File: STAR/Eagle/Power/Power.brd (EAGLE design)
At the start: 51 x 40.4 mm, 46 parts, among them J1 J30J-25, U1 LMR16020, U2 LMR16020, U3 LMR16020

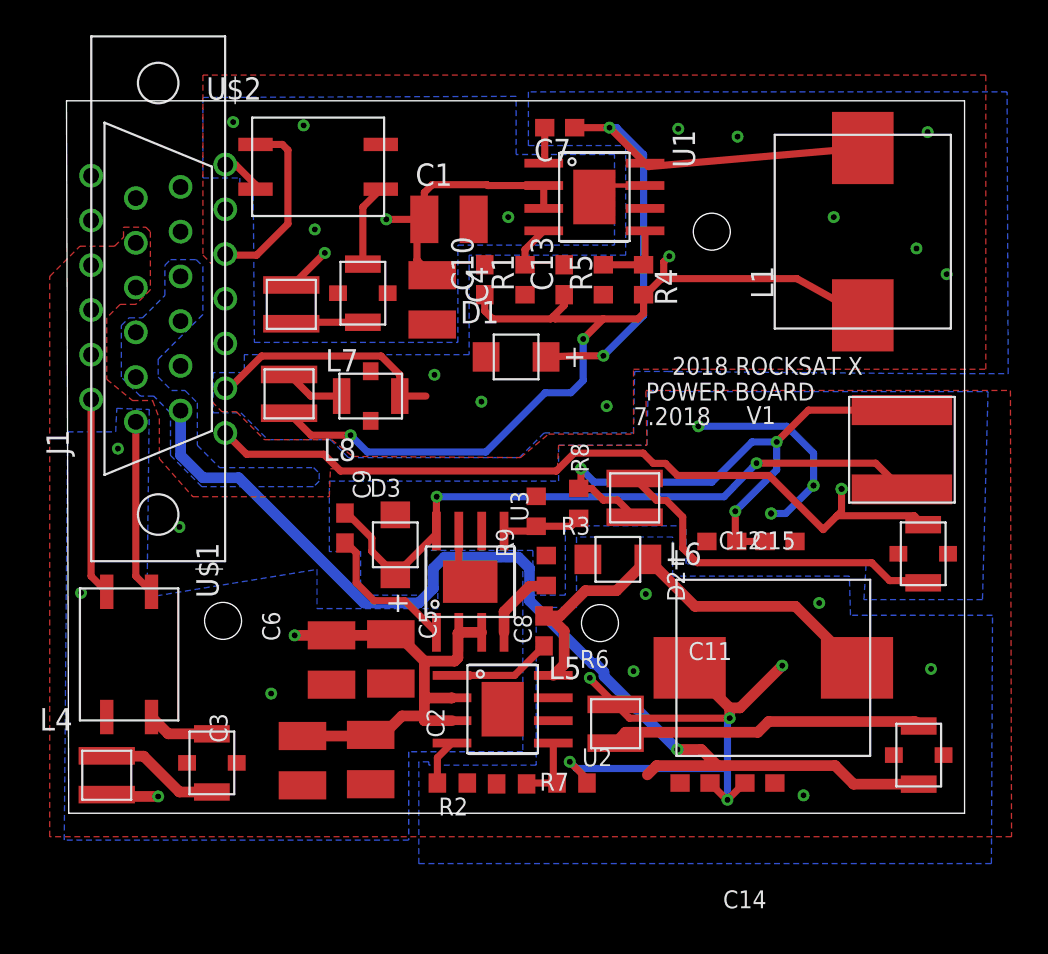
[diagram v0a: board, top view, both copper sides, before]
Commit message: reoriented capacitors on power board
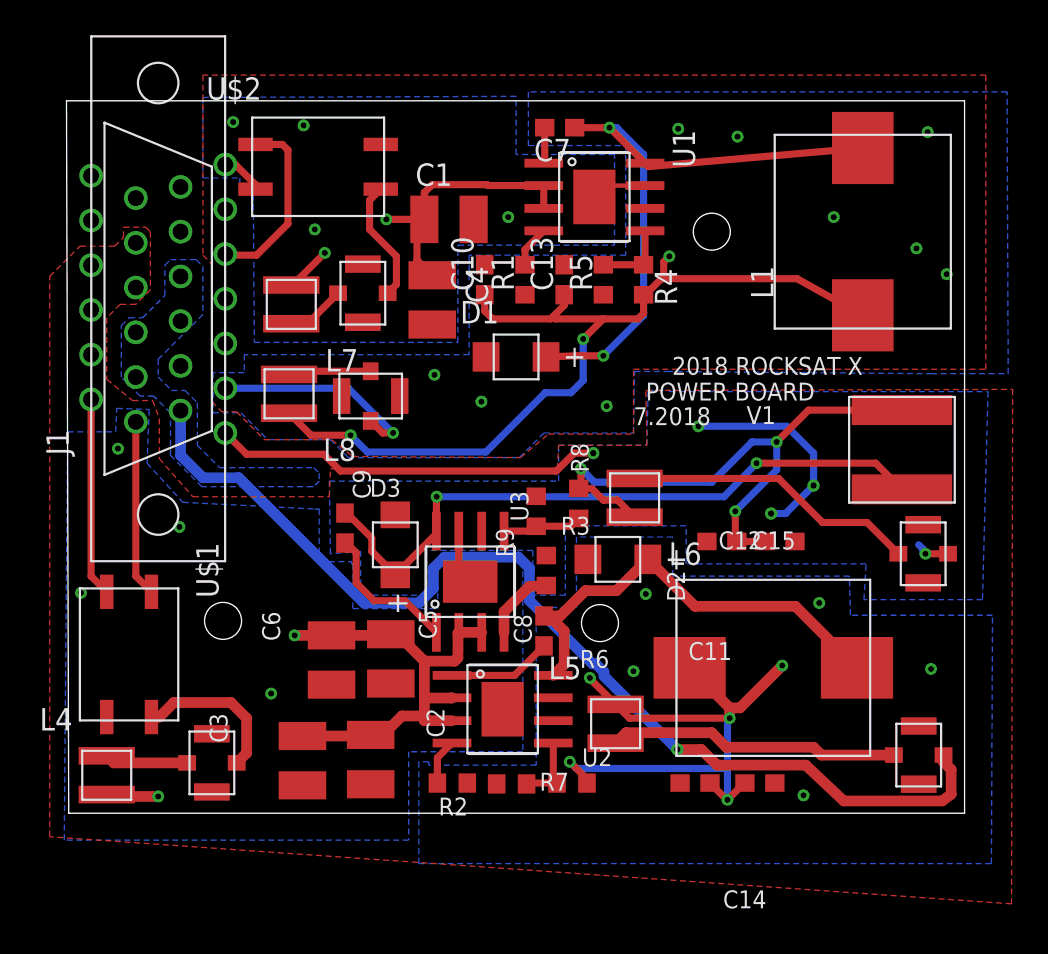
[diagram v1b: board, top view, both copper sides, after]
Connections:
- net 12V_FILT: now also U$7.P$4; no longer U$7.P$3
- net 3V3_FILT: now also U$5.P$4; no longer U$5.P$3
- net 5V_FILT: now also U$4.P$4; no longer U$4.P$2
- net GND: now also U$6.P$2, U$6.P$3; no longer U$6.P$4, U$6.P$5, U$7.P$4, U$7.P$5
- net GSE_GND: now also U$3.P$2, U$3.P$3, U$4.P$2, U$4.P$3, U$5.P$2, U$5.P$3; no longer U$3.P$4, U$3.P$5, U$4.P$4, U$4.P$5, U$5.P$4, U$5.P$5
- net N$28: now also U$1.P$4, U$3.P$4; no longer L4.P$1, U$3.P$2
- net N$29: now also U$6.P$5; no longer U$6.P$2
- net N$31: now also L4.P$1, U$3.P$5; no longer U$1.P$4, U$3.P$3
- net N$32: now also U$4.P$5; no longer U$4.P$3
- net N$33: now also U$5.P$5; no longer U$5.P$2
- net N$34: now also U$6.P$4; no longer U$6.P$3
- net N$35: now also U$7.P$5; no longer U$7.P$2
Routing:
- net 3V3_FILT: track 44.9 -> 24.2 mm, vias 1 -> 2
- net N$33: track 19.9 -> 16.7 mm
- net N$29: track 4.68 -> 7.00 mm
- net N$28: track 6.82 -> 8.88 mm
- net 12V_FILT: track 13.8 -> 12.1 mm, vias 0 -> 7
- net N$32: track 17.8 -> 16.6 mm
- net N$35: track 3.49 -> 4.71 mm
- net N$31: track 3.82 -> 4.73 mm
- net N$34: track 4.10 -> 3.37 mm
- net 5V_FILT: track 60.4 -> 61.0 mm
- added copper zone on layer 16, net 12V_FILT
- removed copper zone on layer 16, net +12V_FILT

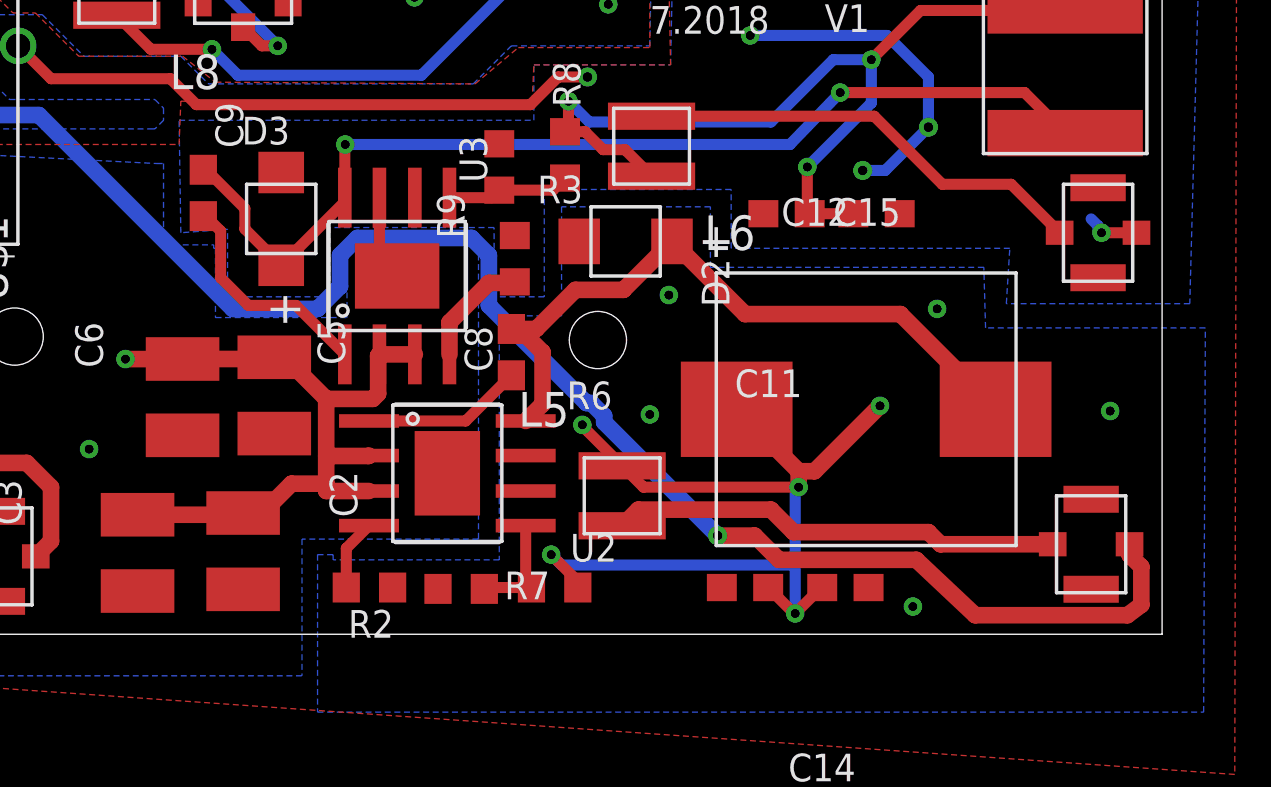
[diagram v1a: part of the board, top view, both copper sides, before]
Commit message: Fixed an air wire on the ground lines and a non-connection in the sketch
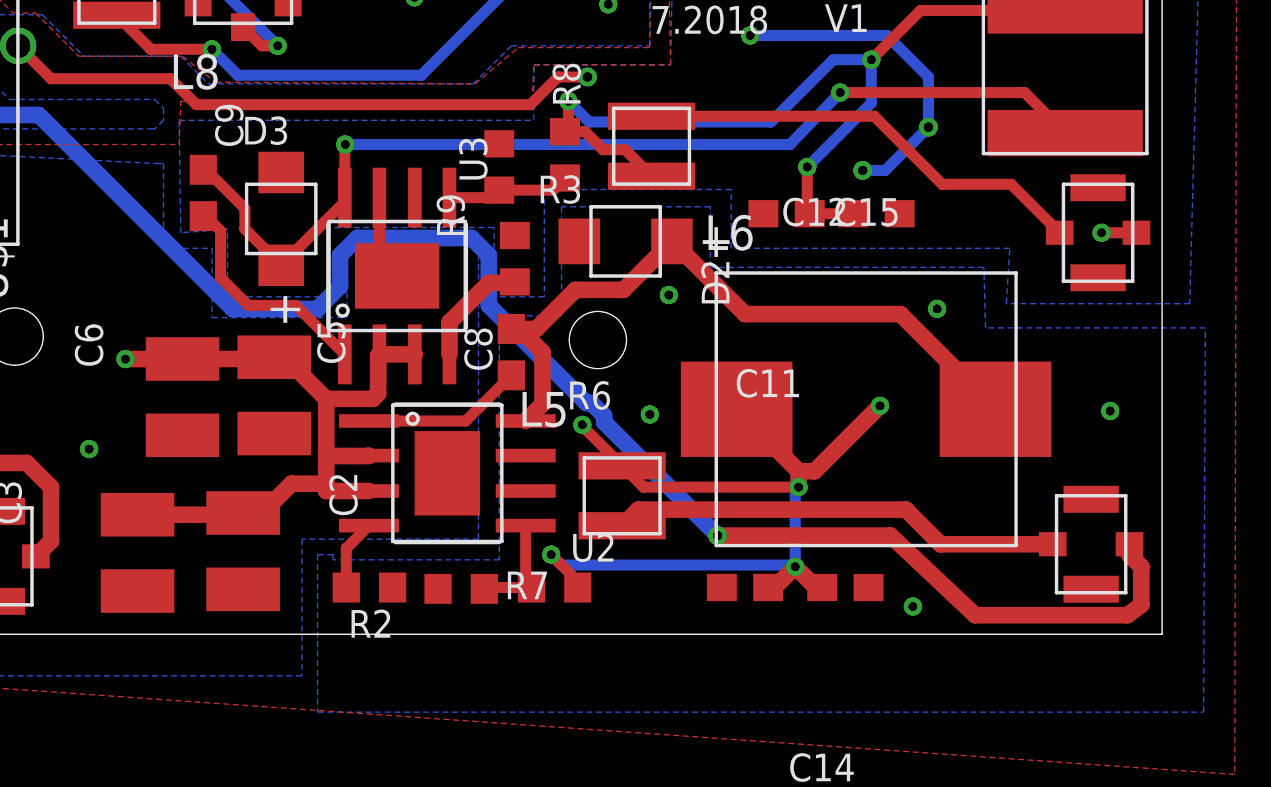
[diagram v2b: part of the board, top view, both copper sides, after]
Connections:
- removed net N$38: U$1.P$3
- net GND: now also U$7.P$3
- net GSE_GND: now also U$1.P$3
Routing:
- net +5V: track 34.9 -> 33.0 mm
- net 3V3_FILT: track 24.2 -> 23.5 mm
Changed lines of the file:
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@@
 <?xml version="1.0" encoding="utf-8"?>
 <!DOCTYPE eagle SYSTEM "eagle.dtd">
-<eagle version="7.6.0">
+<eagle version="9.1.0">
 <drawing>
 <settings>
 <setting alwaysvectorfont="no"/>
+<setting keepoldvectorfont="yes"/>
 <setting verticaltext="up"/>
 </settings>
@@
 <param name="dpMaxLengthDifference" value="10mm"/>
 <param name="dpGapFactor" value="2.5"/>
-<param name="checkGrid" value="0"/>
 <param name="checkAngle" value="0"/>
 <param name="checkFont" value="1"/>
 <param name="checkRestrict" value="1"/>
+<param name="checkStop" value="0"/>
+<param name="checkValues" value="0"/>
+<param name="checkNames" value="1"/>
+<param name="checkWireStubs" value="1"/>
+<param name="checkPolygonWidth" value="0"/>
 <param name="useDiameter" value="13"/>
 <param name="maxErrors" value="50"/>
@@
 <contactref element="U$6" pad="P$2"/>
 <contactref element="U$6" pad="P$3"/>
+<contactref element="U$7" pad="P$3"/>
 </signal>
 <signal name="N$1">
@@
 <via x="23.241" y="1.3335" extent="1-16" drill="0.3302"/>
 <via x="22.098" y="-3.429" extent="1-16" drill="0.3302"/>
-<via x="31.0515" y="-5.588" extent="1-16" drill="0.3302"/>
+<via x="31.0515" y="-3.8735" extent="1-16" drill="0.3302"/>
 <via x="34.163" y="2.032" extent="1-16" drill="0.3302"/>
 <wire x1="23.075" y1="-4.6355" x2="23.075" y2="-4.406" width="0.4064" layer="1"/>
@@
 <wire x1="23.241" y1="1.3335" x2="23.3885" y2="1.143" width="0.4064" layer="1"/>
 <wire x1="23.3885" y1="1.143" x2="24.7015" y2="-0.17" width="0.4064" layer="1"/>
-<wire x1="30.06" y1="-4.6355" x2="31.0125" y2="-5.588" width="0.4064" layer="1"/>
-<wire x1="31.0125" y1="-5.588" x2="31.0515" y2="-5.588" width="0.4064" layer="1"/>
-<wire x1="31.0515" y1="-5.588" x2="32.004" y2="-4.6355" width="0.4064" layer="1"/>
-<wire x1="32.004" y1="-4.6355" x2="32.043" y2="-4.6355" width="0.4064" layer="1"/>
 <wire x1="31.1785" y1="-0.9525" x2="31.0515" y2="-1.0795" width="0.4064" layer="16"/>
 <wire x1="31.0515" y1="-1.0795" x2="31.0515" y2="-3.81" width="0.4064" layer="16"/>
-<wire x1="31.0515" y1="-3.81" x2="31.0515" y2="-5.588" width="0.4064" layer="16"/>
+<wire x1="31.0515" y1="-3.81" x2="31.0515" y2="-3.8735" width="0.4064" layer="16"/>
 <wire x1="24.7015" y1="-0.17" x2="25.484" y2="-0.9525" width="0.4064" layer="1"/>
 <wire x1="25.484" y1="-0.9525" x2="31.1785" y2="-0.9525" width="0.4064" layer="1"/>
@@
 <wire x1="34.163" y1="2.032" x2="31.7625" y2="-0.3685" width="0.6096" layer="1"/>
 <wire x1="31.7625" y1="-0.3685" x2="31.1785" y2="-0.3685" width="0.6096" layer="1"/>
+<wire x1="31.0515" y1="-3.8735" x2="31.8135" y2="-4.6355" width="0.6096" layer="1"/>
+<wire x1="31.8135" y1="-4.6355" x2="32.043" y2="-4.6355" width="0.6096" layer="1"/>
+<wire x1="31.0515" y1="-3.8735" x2="30.2895" y2="-4.6355" width="0.6096" layer="1"/>
+<wire x1="30.2895" y1="-4.6355" x2="30.06" y2="-4.6355" width="0.6096" layer="1"/>
 </signal>
 <signal name="N$11">
@@
 <vertex x="7.62" y="10.922"/>
 <vertex x="7.874" y="10.922"/>
-<vertex x="7.874" y="7.9375"/>
-<vertex x="9.7155" y="7.9375"/>
-<vertex x="9.7155" y="7.8105"/>
-<vertex x="9.779" y="7.8105"/>
-<vertex x="9.779" y="5.2705"/>
+<vertex x="7.874" y="7.8105"/>
+<vertex x="9.652" y="7.8105"/>
+<vertex x="9.652" y="7.8105"/>
+<vertex x="9.652" y="5.2705"/>
 <vertex x="14.605" y="5.2705"/>
 <vertex x="14.605" y="7.9375"/>
@@
 <wire x1="19.812" y1="5.715" x2="19.812" y2="7.5565" width="0.6096" layer="16"/>
 <via x="28.2054875" y="-2.7305" extent="1-16" drill="0.35"/>
-<wire x1="28.2054875" y1="-2.7305" x2="29.5656" y2="-2.7305" width="0.6096" layer="1"/>
-<wire x1="29.5656" y1="-2.7305" x2="30.4546" y2="-3.6195" width="0.6096" layer="1"/>
 <wire x1="3.302" y1="12.7" x2="1.27" y2="12.7" width="0.6096" layer="16"/>
 <wire x1="1.27" y1="12.7" x2="0" y2="13.97" width="0.6096" layer="16"/>
@@
 <wire x1="43.7515" y1="-5.2705" x2="43.2435" y2="-5.6515" width="0.6096" layer="1"/>
 <wire x1="43.2435" y1="-5.6515" x2="37.6555" y2="-5.6515" width="0.6096" layer="1"/>
-<wire x1="37.6555" y1="-5.6515" x2="35.4965" y2="-3.6195" width="0.6096" layer="1"/>
-<wire x1="35.4965" y1="-3.6195" x2="30.4546" y2="-3.6195" width="0.6096" layer="1"/>
+<wire x1="37.6555" y1="-5.6515" x2="34.5519375" y2="-2.7305" width="0.6096" layer="1"/>
+<wire x1="34.5519375" y1="-2.7305" x2="28.2054875" y2="-2.7305" width="0.6096" layer="1"/>
 </signal>
 <signal name="3V3_FILT">
@@
 <wire x1="43.5737" y1="8.382" x2="42.291" y2="8.382" width="0.4064" layer="1"/>
 <via x="42.291" y="8.382" extent="1-16" drill="0.3302"/>
-<wire x1="42.291" y1="8.382" x2="42.2275" y2="8.382" width="0.4064" layer="16"/>
-<wire x1="42.2275" y1="8.382" x2="42.164" y2="8.4455" width="0.4064" layer="16"/>
-<wire x1="42.164" y1="8.4455" x2="42.164" y2="8.636" width="0.4064" layer="16"/>
-<wire x1="42.164" y1="8.636" x2="41.91" y2="8.89" width="0.4064" layer="16"/>
 <wire x1="22.352" y1="14.097" x2="23.4315" y2="14.097" width="0.4064" layer="1"/>
 </signal>
@@
 <contactref element="U$5" pad="P$3"/>
 <contactref element="U$5" pad="P$2"/>
-<wire x1="33.743" y1="-4.6355" x2="28.36" y2="-4.6355" width="0" layer="19" extent="1-1"/>
+<contactref element="U$1" pad="P$3"/>
 </signal>
 <signal name="TE_UFILT">
@@
 <signal name="H">
 <contactref element="J1" pad="12"/>
-</signal>
-<signal name="N$38">
-<contactref element="U$1" pad="P$3"/>
 </signal>
 <signal name="N$28">
@@
 <contactref element="L5" pad="P$2"/>
 <wire x1="40.5003" y1="-3.048" x2="36.3855" y2="-3.048" width="0.6096" layer="1"/>
-<wire x1="36.3855" y1="-3.048" x2="35.941" y2="-2.6035" width="0.6096" layer="1"/>
-<wire x1="35.941" y1="-2.6035" x2="30.988" y2="-2.6035" width="0.6096" layer="1"/>
-<wire x1="30.988" y1="-2.6035" x2="30.1625" y2="-1.778" width="0.6096" layer="1"/>
-<wire x1="30.1625" y1="-1.778" x2="25.2935" y2="-1.778" width="0.6096" layer="1"/>
+<wire x1="36.3855" y1="-3.048" x2="35.1155" y2="-1.778" width="0.6096" layer="1"/>
+<wire x1="35.1155" y1="-1.778" x2="25.2935" y2="-1.778" width="0.6096" layer="1"/>
 <wire x1="25.2935" y1="-1.778" x2="24.7015" y2="-2.37" width="0.6096" layer="1"/>
 </signal>
@@
 </signal>
 </signals>
-<errors>
-</errors>
+<mfgpreviewcolors>
+<mfgpreviewcolor name="soldermaskcolor" color="0xC8008000"/>
+<mfgpreviewcolor name="silkscreencolor" color="0xFFFEFEFE"/>
+<mfgpreviewcolor name="backgroundcolor" color="0xFF282828"/>
+<mfgpreviewcolor name="coppercolor" color="0xFFFFBF00"/>
+<mfgpreviewcolor name="substratecolor" color="0xFF786E46"/>
+</mfgpreviewcolors>
 </board>
 </drawing>
